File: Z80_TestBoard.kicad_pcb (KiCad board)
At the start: 2 copper layers, 68.5 x 91.9 mm, 40 parts, among them J1 LEFT, J2 RIGHT, J3 PWR, J5 CLK_SW, J6 LED_01x03, J7 USB_B_Mini, J8 USB_B_Mini, SW1 RESET, SW2 ON|OFF, SW3 PICK COLOR, U1 Z84C00_PLCC, U2 NE555P, U3 IS65C256AL

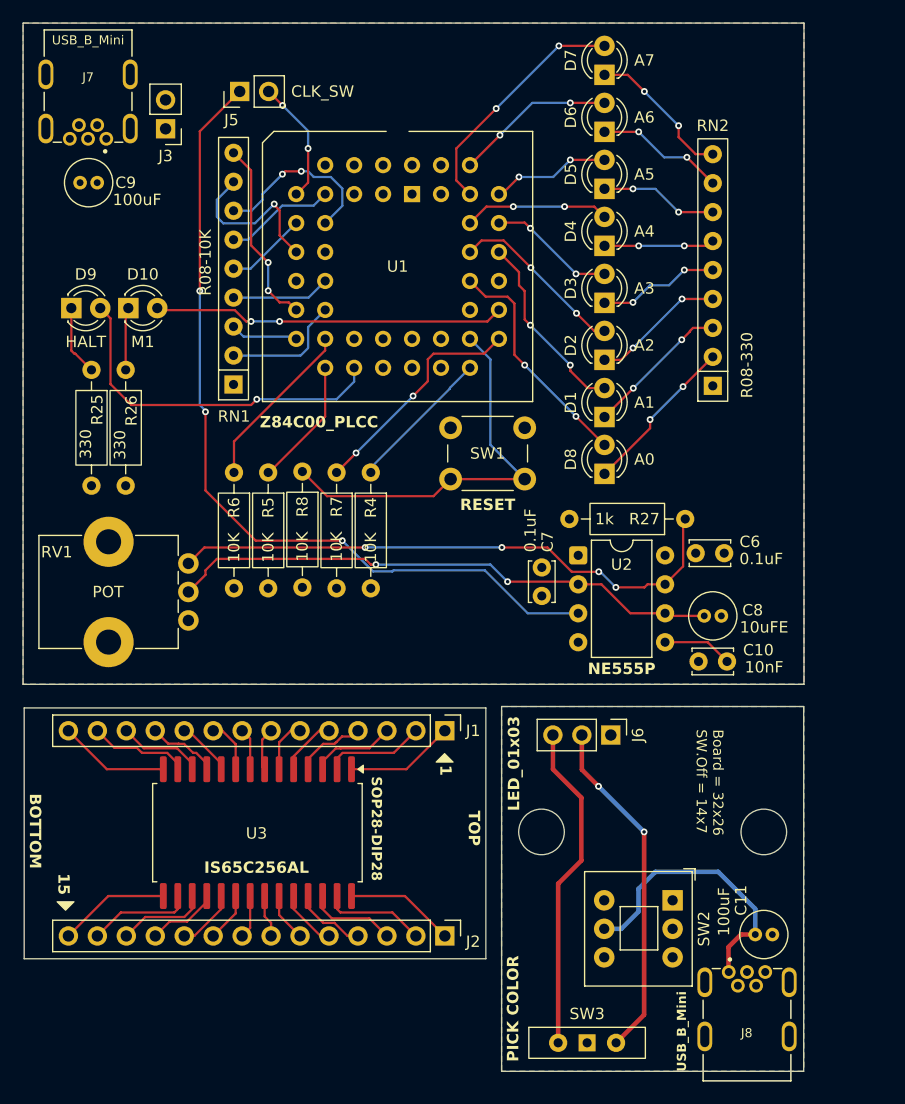
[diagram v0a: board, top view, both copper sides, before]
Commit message: production-ready panelized pcb.
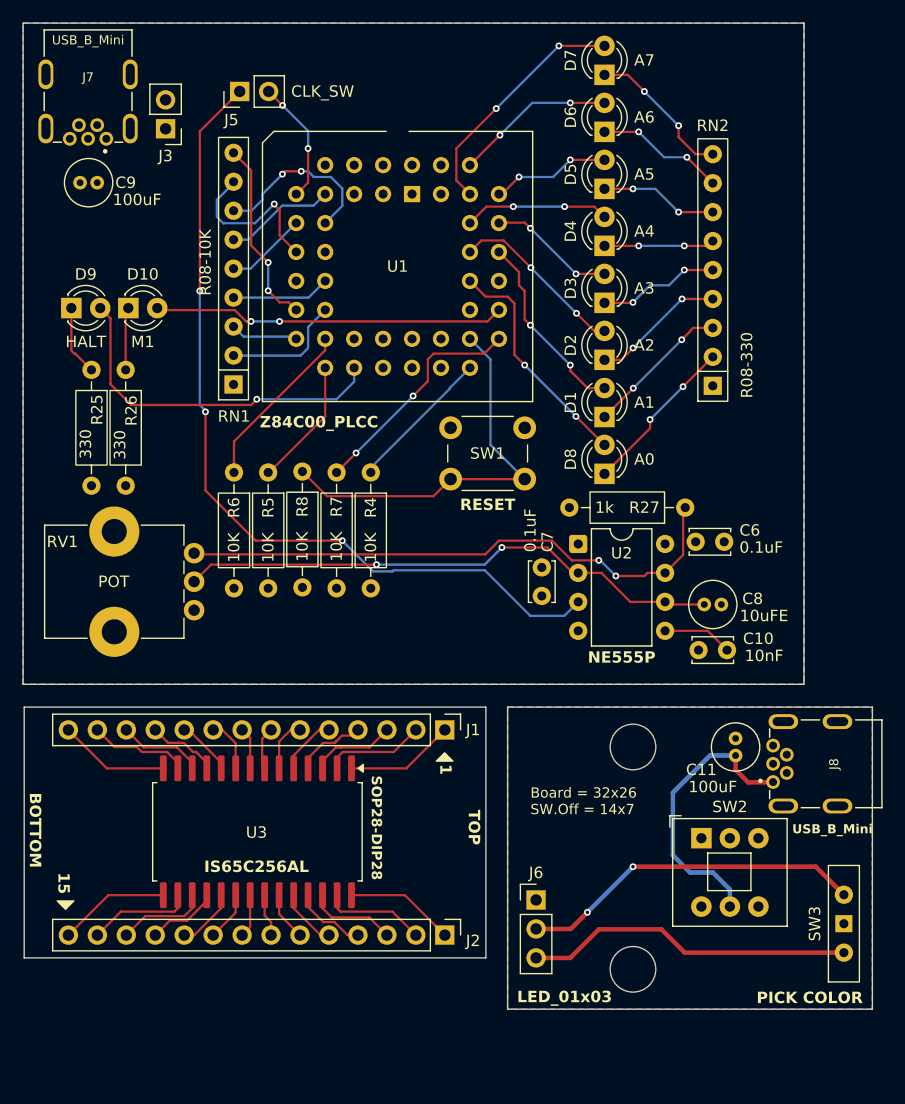
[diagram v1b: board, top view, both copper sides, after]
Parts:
- moved SW3 24.8 mm to (183.5, 133.0), turned to 90 degrees
- moved J8 19.4 mm to (178.2, 119.0), turned to -90 degrees
- moved C11 17.5 mm to (174.0, 116.8), turned to -90 degrees
- moved J6 15.9 mm to (156.5, 130.9), turned to 0 degrees
- moved SW2 6.01 mm to (171.0, 125.5), turned to 0 degrees
- moved RV1 1.03 mm to (126.5, 100.5)
- moved C10 1.00 mm to (173.2, 109.0)
- moved C6 1.00 mm to (170.5, 99.5)
- moved C8 1.00 mm to (171.2, 105.0)
- moved R27 1.00 mm to (169.6, 96.5)
- moved U2 1.00 mm to (160.2, 99.7)
- moved J1 0.08 mm to (148.5, 116.0)
- moved U3 0.08 mm to (132.1, 124.9)
- moved J2 0.07 mm to (148.5, 134.0)
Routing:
- net Net-(U2-THRES): track 48.8 -> 47.8 mm
- net Net-(U2-DISCH): track 50.4 -> 49.7 mm, vias 4 -> 2
- net /Root/555_CLK: track 73.9 -> 74.5 mm
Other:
- board size 68.5 x 91.9 mm -> 74.5 x 86.5 mm

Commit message: exclude sop28 + led boards.
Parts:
- removed C11: 100uF, Capacitor_THT:C_Radial_D4.0mm_H5.0mm_P1.50mm
- removed J1: LEFT, Connector_PinHeader_2.54mm:PinHeader_1x14_P2.54mm_Vertical
- removed J2: RIGHT, Connector_PinHeader_2.54mm:PinHeader_1x14_P2.54mm_Vertical
- removed J6: LED_01x03, Connector_PinHeader_2.54mm:PinHeader_1x03_P2.54mm_Vertical
- removed J8: USB_B_Mini, Connector_USB:USB_MINI_B_90_Angled
- removed SW2: ON|OFF, Button_Switch_THT:SW_Push_2P2T_Toggle_CK_PVA2OAH5xxxxxxV2
- removed SW3: PICK COLOR, Button_Switch_THT:SW_Slide-03_Wuerth-WS-SLTV_10x2.5x6.4_P2.54mm
- removed U3: IS65C256AL, Package_SO:SOP-28_8.4x18.16mm_P1.27mm
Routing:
- net /LED_Board/LED_V1-: track 30.3 -> 0.00 mm, vias 2 -> 0
- net /LED_Board/LED_V2-: track 28.9 -> 0.00 mm
- net Net-(J8-VBUS): track 25.0 -> 0.00 mm
- net /SOP28-DIP28/IO_3: track 9.77 -> 0.00 mm
- net /SOP28-DIP28/GND3: track 9.72 -> 0.00 mm
- net /SOP28-DIP28/VCC3: track 9.63 -> 0.00 mm
- net /SOP28-DIP28/A14: track 9.58 -> 0.00 mm
- net /SOP28-DIP28/IO_4: track 9.17 -> 0.00 mm
- net /SOP28-DIP28/WE: track 9.03 -> 0.00 mm
- net /SOP28-DIP28/A12: track 8.86 -> 0.00 mm
- net /SOP28-DIP28/IO_2: track 8.75 -> 0.00 mm
- net /SOP28-DIP28/IO_5: track 7.90 -> 0.00 mm
- net /SOP28-DIP28/A13: track 7.76 -> 0.00 mm
- net /SOP28-DIP28/IO_1: track 7.48 -> 0.00 mm
- net /SOP28-DIP28/A7: track 7.44 -> 0.00 mm
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- removed copper zone on B.Cu, net GND1
- removed copper zone on F.Cu, net VCCQ
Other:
- board size 74.5 x 86.5 mm -> 68.5 x 58 mm
- board text removed: "1"
- board text removed: "15"
- board text removed: "BOTTOM"
- board text removed: "Board = 32x26 SW.Off = 14x7"
- board text removed: "SOP28-DIP28"
- board text removed: "TOP"
